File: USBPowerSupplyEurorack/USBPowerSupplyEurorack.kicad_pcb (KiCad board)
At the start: 2 copper layers, 9.8 x 110 mm, 19 parts, among them J1 1734366-1, J2 10129381-910001BLF, Q1 Q_PMOS_GSD

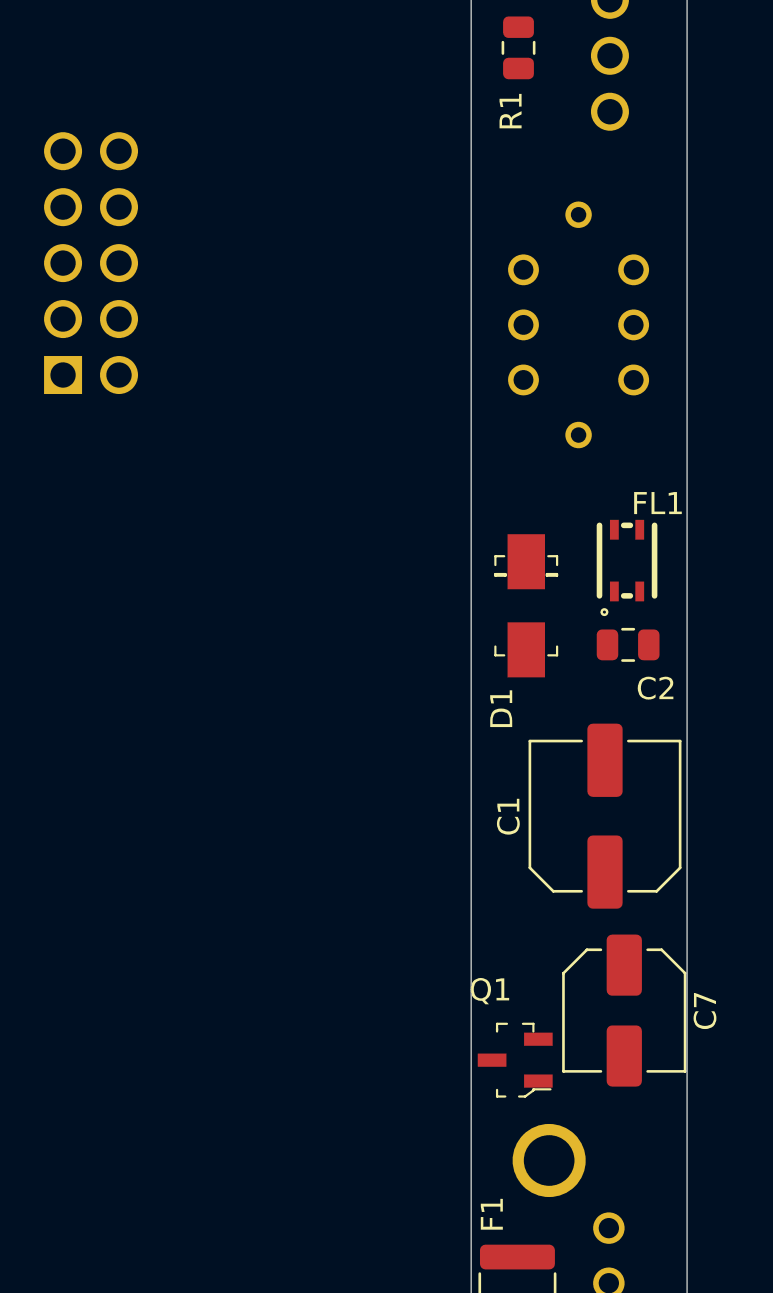
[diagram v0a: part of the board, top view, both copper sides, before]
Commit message: replaced power header for SMT, finished placement
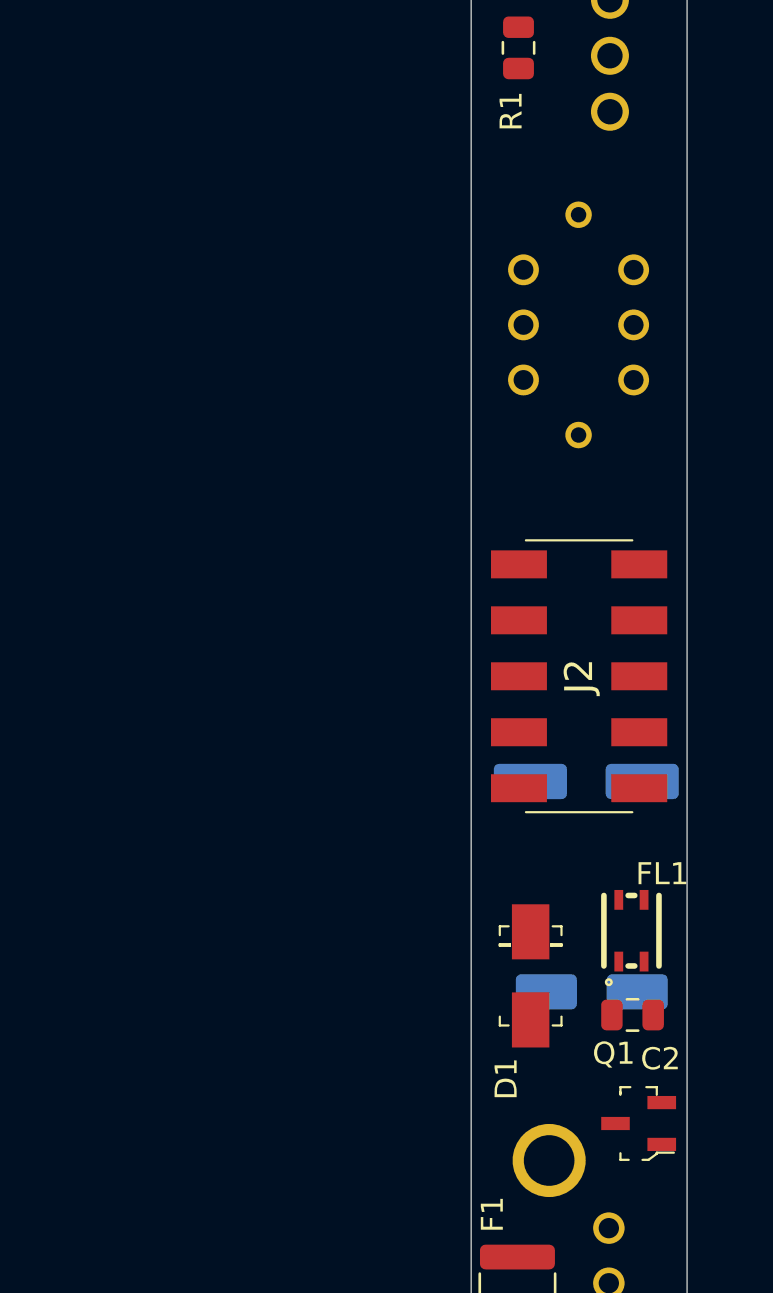
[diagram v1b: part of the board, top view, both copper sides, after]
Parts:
- C1, C7: moved to B.Cu
- J2: value 10129381-910001BLF -> 95278-501A10LF; footprint 10129381-910001BLF:HDRV10W67P254_2X5_1270X483X858P -> 95278-501A10LF:95278501A10LF; moved to F.Cu
- moved J2 27.1 mm to (139.4, 120.5)
- moved C2 16.8 mm to (141.9, 135.9)
- moved D1 16.8 mm to (137.2, 134.1)
- moved FL1 16.8 mm to (141.8, 132.1)
- moved Q1 6.29 mm to (142.2, 140.8)
- moved C1 1.79 mm to (139.8, 125.3), turned to 0 degrees
- moved C7 1.70 mm to (140.0, 134.8), turned to 0 degrees

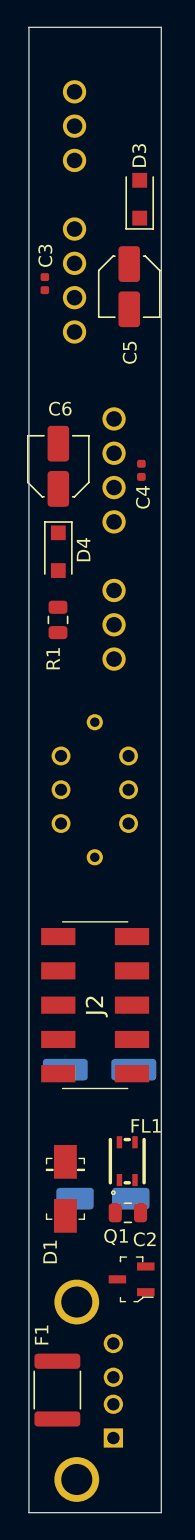
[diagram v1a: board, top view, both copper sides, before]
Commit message: worked a components placement
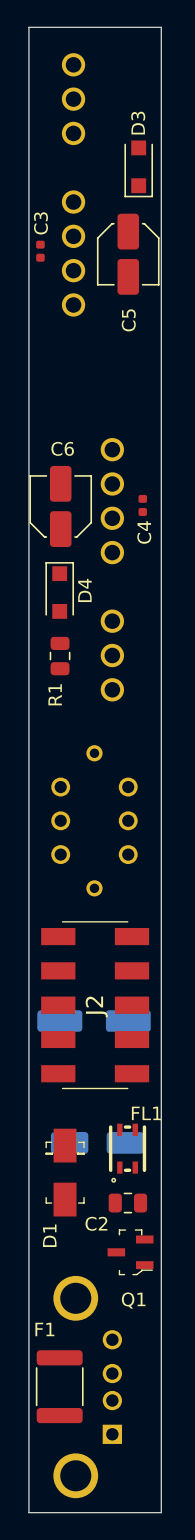
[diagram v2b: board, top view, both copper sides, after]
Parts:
- moved C7 4.14 mm to (139.6, 130.7)
- moved C1 3.62 mm to (139.4, 121.7)
- moved D4 3.03 mm to (136.8, 90.0)
- moved C6 2.98 mm to (136.9, 83.6)
- moved R1 2.68 mm to (136.8, 94.7)
- moved C4 2.60 mm to (143.0, 83.5)
- moved C3 2.42 mm to (135.4, 64.7)
- moved C5 2.40 mm to (141.9, 64.9)
- moved D3 2.40 mm to (142.7, 58.5)
- moved S1 2.30 mm to (136.9, 109.4)
- moved PS2 2.28 mm to (140.7, 97.2)
- moved PS1 2.00 mm to (137.8, 50.9)
- moved Q1 2.00 mm to (142.1, 138.8)
- moved D1 1.20 mm to (137.2, 132.9)
- moved FL1 0.93 mm to (141.8, 131.2)
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
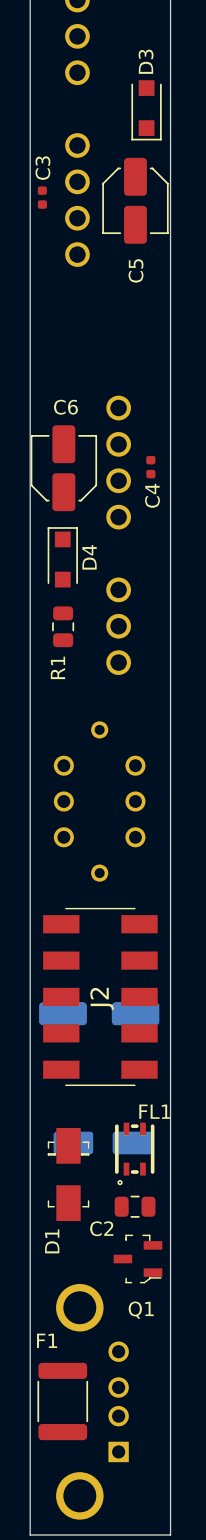
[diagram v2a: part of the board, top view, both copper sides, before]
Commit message: added 3D models
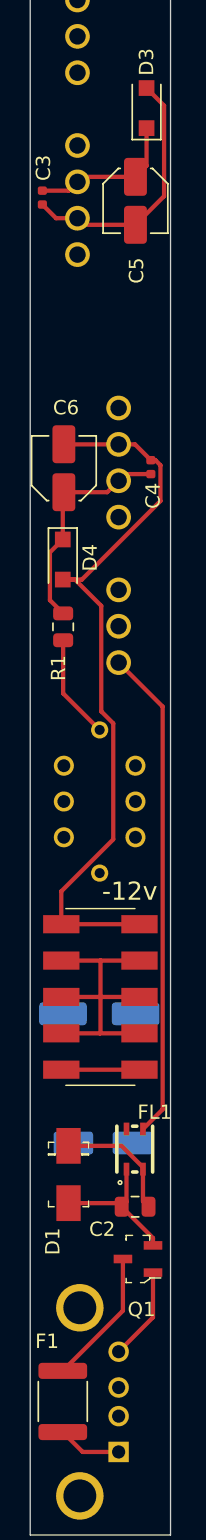
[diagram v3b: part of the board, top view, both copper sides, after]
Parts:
- renumbered J2 to -12v
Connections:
- S1 pad 4: +5V -> +Vin
- S1 pad 5: +5V -> +Vin
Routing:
- net 0V: track 0.00 -> 55.3 mm
- net -12V: track 0.00 -> 51.9 mm
- net -Vin: track 0.00 -> 34.4 mm
- net +12V: track 0.00 -> 16.1 mm
- net GND: track 0.00 -> 15.3 mm
- net Net-(C1-Pad1): track 0.00 -> 10.2 mm
- net +5V: track 0.00 -> 9.55 mm
- net Net-(R1-Pad1): track 0.00 -> 7.32 mm
- net Net-(F1-Pad1): track 0.00 -> 4.47 mm

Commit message: naive routing to try
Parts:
- moved R1 1.90 mm to (136.9, 92.8), turned to 180 degrees
- moved D4 0.84 mm to (137.6, 89.7), turned to 0 degrees
- turned -12v to 270 degrees
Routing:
- net +Vin: track 0.00 -> 107.8 mm, vias 0 -> 1
- net CTRL: track 0.00 -> 58.0 mm
- net +12V: track 16.1 -> 72.2 mm
- net -Vin: track 34.4 -> 84.6 mm, vias 0 -> 1
- net 0V: track 55.3 -> 103.9 mm
- net GND: track 15.3 -> 45.6 mm, vias 0 -> 1
- net Net-(C1-Pad1): track 10.2 -> 28.9 mm, vias 0 -> 1
- net Net-(J1-PadSH1): track 0.00 -> 14.5 mm
- net -12V: track 51.9 -> 60.2 mm
- net Net-(R1-Pad1): track 7.32 -> 9.73 mm
- added copper zone on F.Cu, net 0V
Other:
- outline, holes or cut-outs redrawn

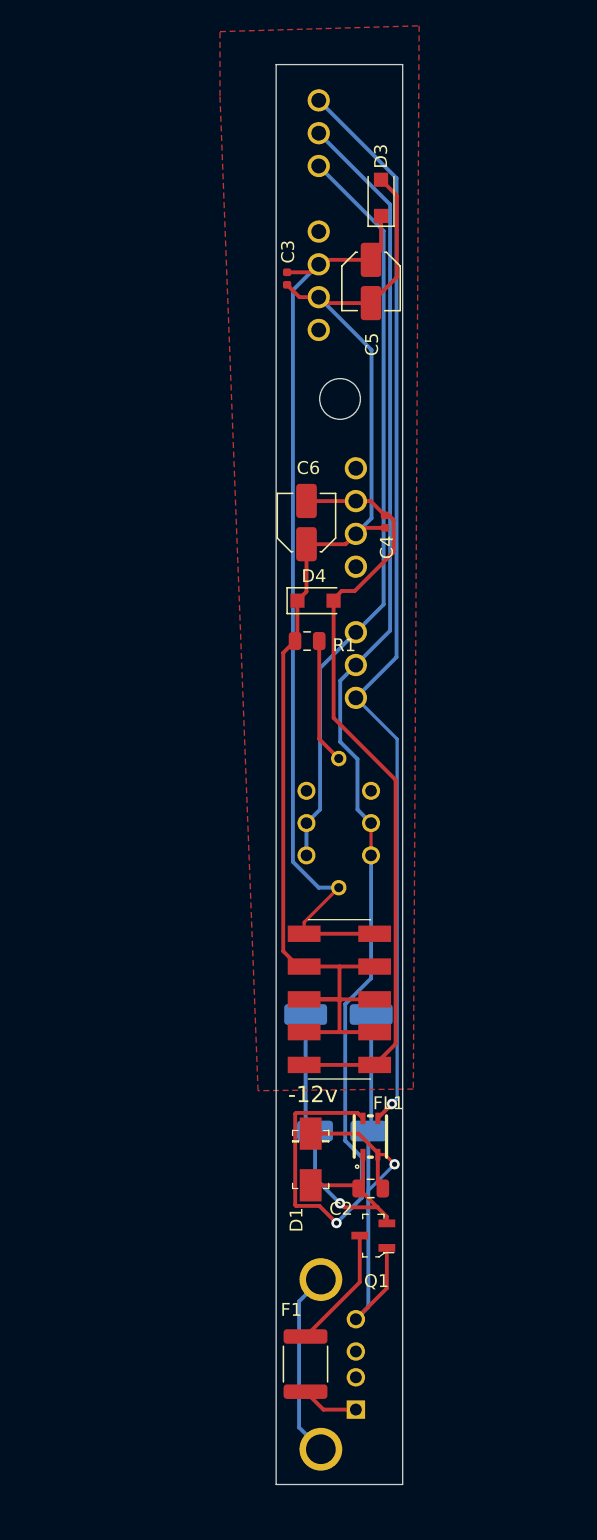
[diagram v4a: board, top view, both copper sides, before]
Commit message: changed footprints placement, added the two LEDs
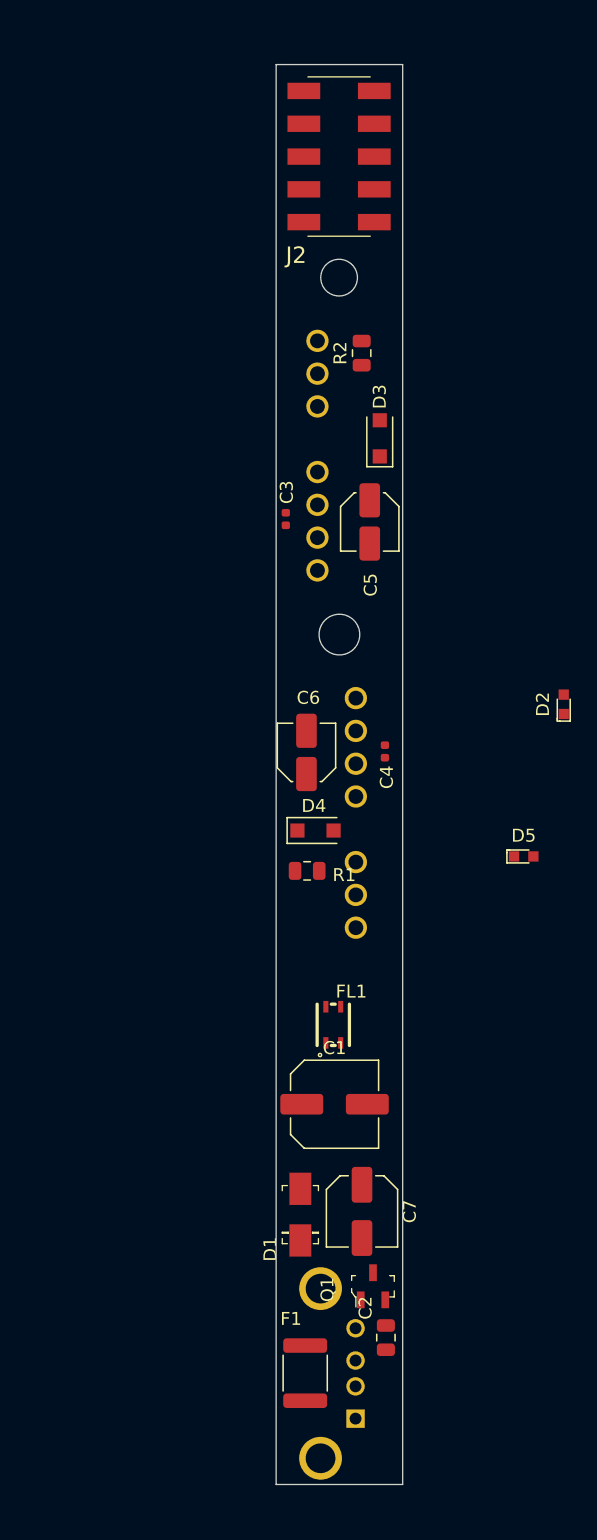
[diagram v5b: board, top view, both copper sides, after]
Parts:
- removed S1: LP4OA1PBCTR, LP4OA1PBCTR:LP4OA1PBCTR
- added D2: Blue, digikey-footprints:LED_0603, F.Cu at (156.8, 97.7)
- added D5: Blue, digikey-footprints:LED_0603, F.Cu at (153.7, 109.5)
- added R2: 1K, Resistor_SMD:R_0805_2012Metric, F.Cu at (141.2, 70.5)
- C1, C7: moved to F.Cu
- R1: value 1.5K -> 1K
- moved J2 65.3 mm to (139.4, 55.2)
- moved PS1 18.6 mm to (137.8, 69.5)
- moved D3 18.6 mm to (142.6, 77.1)
- moved C3 18.6 mm to (135.3, 83.3)
- moved C5 18.6 mm to (141.8, 83.5)
- moved C6 17.8 mm to (136.9, 101.4)
- moved C4 17.8 mm to (143.0, 101.3)
- moved D4 17.8 mm to (137.6, 107.5)
- moved PS2 17.8 mm to (140.7, 115.0)
- moved R1 17.8 mm to (136.9, 110.6)
- moved C2 11.6 mm to (143.1, 146.7), turned to 270 degrees
- moved FL1 9.12 mm to (139.0, 122.5)
- moved C1 6.96 mm to (139.1, 128.7)
- moved C7 6.42 mm to (141.2, 136.9), turned to 270 degrees
- moved D1 4.35 mm to (136.4, 137.2), turned to 90 degrees
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- renumbered -12v to J2
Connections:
- J1 pad SH1: Net-(J1-PadSH1) -> GND
- J1 pad SH2: Net-(J1-PadSH1) -> GND
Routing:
- net +Vin: track 107.8 -> 0.00 mm, vias 1 -> 0
- net 0V: track 103.9 -> 0.00 mm
- net -Vin: track 84.6 -> 0.00 mm, vias 1 -> 0
- net +12V: track 72.2 -> 0.00 mm
- net -12V: track 60.2 -> 0.00 mm
- net CTRL: track 58.0 -> 0.00 mm
- net GND: track 45.6 -> 0.00 mm, vias 1 -> 0
- net Net-(C1-Pad1): track 28.9 -> 0.00 mm, vias 1 -> 0
- net Net-(J1-PadSH1): track 14.5 -> 0.00 mm
- net Net-(D2-Pad1): track 9.73 -> 0.00 mm
- net +5V: track 9.55 -> 0.00 mm
- net Net-(F1-Pad1): track 4.47 -> 0.00 mm
- removed copper zone on F.Cu, net 0V
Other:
- outline, holes or cut-outs redrawn

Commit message: added LEDs, all components are placed now
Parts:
- D2, D5: moved to B.Cu
- moved D2 43.5 mm to (139.4, 57.8), turned to 0 degrees
- moved D5 21.1 mm to (139.4, 125.0), turned to 180 degrees

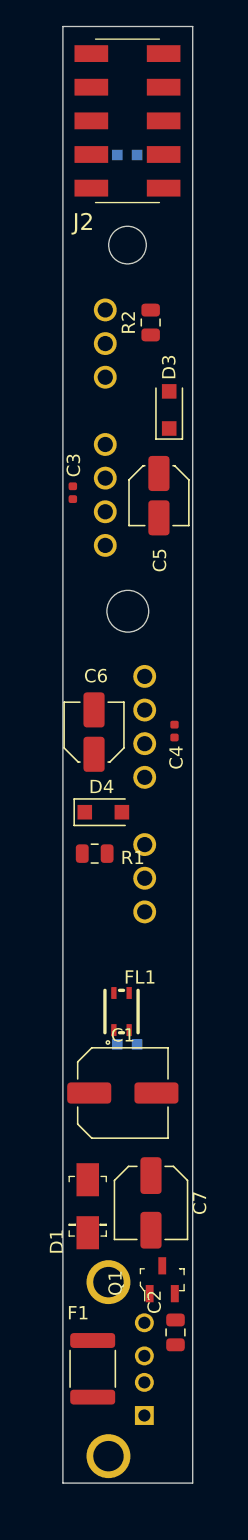
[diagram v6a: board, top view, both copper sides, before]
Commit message: new naive routing
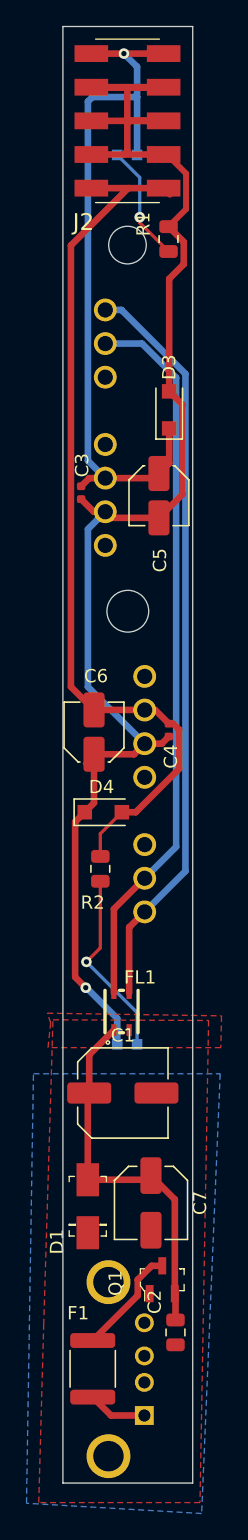
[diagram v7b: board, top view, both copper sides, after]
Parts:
- moved R1 46.7 mm to (142.5, 64.2), turned to 90 degrees
- moved R2 41.4 mm to (137.4, 111.7)
- moved C3 0.62 mm to (135.9, 83.3)
- moved C4 0.43 mm to (142.6, 101.2)
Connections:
- PS1 pad 3: CTRL -> Net-(PS1-Pad3)
- PS2 pad 3: CTRL -> Net-(PS2-Pad3)
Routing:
- net 0V: track 0.00 -> 118.4 mm, vias 0 -> 1
- net -12V: track 0.00 -> 67.7 mm
- net -Vin: track 0.00 -> 56.6 mm
- net +12V: track 0.00 -> 56.4 mm, vias 0 -> 1
- net +Vin: track 0.00 -> 54.8 mm
- net Net-(C1-Pad1): track 0.00 -> 28.7 mm
- net Net-(D5-Pad1): track 0.00 -> 14.3 mm, vias 0 -> 1
- net Net-(D2-Pad1): track 0.00 -> 8.89 mm, vias 0 -> 1
- net +5V: track 0.00 -> 8.28 mm
- net Net-(F1-Pad1): track 0.00 -> 4.47 mm
- added copper zone on B.Cu, net GND
- added copper zone on F.Cu, net GND

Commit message: final placement
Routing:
- removed copper zone on B.Cu, net GND
- removed copper zone on F.Cu, net GND
